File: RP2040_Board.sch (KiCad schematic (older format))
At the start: 1 part, among them U2 Pico

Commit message: Previous current input circuit was reaching op amp saturation. Possible solution may involve transistor, but for now, higher power supply is sufficient.
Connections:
- net labels added: +10V, 10V
- wire segments 12 -> 15
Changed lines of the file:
@@
 F3 "OUT" I R 7250 4050 50
 $EndSheet
+Text GLabel 2200 3550 1    50   Input ~ 0
+10V
+$Comp
+L power:PWR_FLAG #FLG?
+U 1 1 60AEFCD1
+P 2300 3600
+F 0 "#FLG?" H 2300 3675 50  0001 C CNN
+F 1 "PWR_FLAG" V 2300 3728 50  0000 L CNN
+F 2 "" H 2300 3600 50  0001 C CNN
+F 3 "~" H 2300 3600 50  0001 C CNN
+	1    2300 3600
+	0    1    1    0
+$EndComp
+$Comp
+L power:+10V #PWR?
+U 1 1 60AEFE56
+P 2200 3650
+F 0 "#PWR?" H 2200 3500 50  0001 C CNN
+F 1 "+10V" H 2215 3823 50  0000 C CNN
+F 2 "" H 2200 3650 50  0001 C CNN
+F 3 "" H 2200 3650 50  0001 C CNN
+	1    2200 3650
+	-1   0    0    1
+$EndComp
+Wire Wire Line
+	2200 3550 2200 3600
+Wire Wire Line
+	2300 3600 2200 3600
+Connection ~ 2200 3600
+Wire Wire Line
+	2200 3600 2200 3650
 $EndSCHEMATC

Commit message: Added Optically Isolated Digital Input
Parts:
- added J1: V_OUT, symbol Connector:Conn_01x02_Female
- added J2, J?: mA_OUT, symbol Connector:Conn_01x02_Female
- added J3: mA_IN, Connector_PinSocket_1.00mm:PinSocket_1x02_P1.00mm_Vertical, symbol Connector:Conn_01x02_Female
- added J4: V_IN, symbol Connector:Conn_01x02_Female
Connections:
- net labels added: +3.3V, 3.3V
- wire segments 15 -> 66
- no-connect marks 0 -> 36

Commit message: Comments and Notation for clarity
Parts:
- gave numbers to parts that had none: 1
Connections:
- net labels removed: +10V, 10V
- wire segments 66 -> 65
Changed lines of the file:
@@
 L power:+24V #PWR0102
 U 1 1 60A8325F
-P 1450 3000
-F 0 "#PWR0102" H 1450 2850 50  0001 C CNN
-F 1 "+24V" H 1465 3173 50  0000 C CNN
-F 2 "" H 1450 3000 50  0001 C CNN
-F 3 "" H 1450 3000 50  0001 C CNN
-	1    1450 3000
-	1    0    0    -1
-$EndComp
-Text GLabel 1450 3100 3    50   Input ~ 0
+P 1050 3250
+F 0 "#PWR0102" H 1050 3100 50  0001 C CNN
+F 1 "+24V" H 1065 3423 50  0000 C CNN
+F 2 "" H 1050 3250 50  0001 C CNN
+F 3 "" H 1050 3250 50  0001 C CNN
+	1    1050 3250
+	1    0    0    -1
+$EndComp
+Text GLabel 1050 3350 3    50   Input ~ 0
 24V
 Text GLabel 1050 3800 1    50   Input ~ 0
 GND
 Wire Wire Line
-	1450 3000 1450 3050
+	1050 3250 1050 3300
 Wire Wire Line
 	1050 3900 1050 3850
@@
 L power:PWR_FLAG #FLG0101
 U 1 1 60A8412B
-P 1550 3050
-F 0 "#FLG0101" H 1550 3125 50  0001 C CNN
-F 1 "PWR_FLAG" V 1550 3178 50  0000 L CNN
-F 2 "" H 1550 3050 50  0001 C CNN
-F 3 "~" H 1550 3050 50  0001 C CNN
-	1    1550 3050
+P 1150 3300
+F 0 "#FLG0101" H 1150 3375 50  0001 C CNN
+F 1 "PWR_FLAG" V 1150 3428 50  0000 L CNN
+F 2 "" H 1150 3300 50  0001 C CNN
+F 3 "~" H 1150 3300 50  0001 C CNN
+	1    1150 3300
 	0    1    1    0
 $EndComp
@@
 $EndComp
 Wire Wire Line
-	1550 3050 1450 3050
-Connection ~ 1450 3050
-Wire Wire Line
-	1450 3050 1450 3100
+	1150 3300 1050 3300
+Connection ~ 1050 3300
+Wire Wire Line
+	1050 3300 1050 3350
 Wire Wire Line
 	1150 3850 1050 3850
@@
 L power:+5V #PWR0103
 U 1 1 60A9FB68
-P 2150 3000
-F 0 "#PWR0103" H 2150 2850 50  0001 C CNN
-F 1 "+5V" H 2165 3173 50  0000 C CNN
-F 2 "" H 2150 3000 50  0001 C CNN
-F 3 "" H 2150 3000 50  0001 C CNN
-	1    2150 3000
-	1    0    0    -1
-$EndComp
-Text GLabel 2150 3100 3    50   Input ~ 0
+P 1800 3250
+F 0 "#PWR0103" H 1800 3100 50  0001 C CNN
+F 1 "+5V" H 1815 3423 50  0000 C CNN
+F 2 "" H 1800 3250 50  0001 C CNN
+F 3 "" H 1800 3250 50  0001 C CNN
+	1    1800 3250
+	1    0    0    -1
+$EndComp
+Text GLabel 1800 3350 3    50   Input ~ 0
 5V
 Wire Wire Line
-	2150 3000 2150 3050
+	1800 3250 1800 3300
 $Comp
 L power:PWR_FLAG #FLG0103
 U 1 1 60AA0BC3
-P 2250 3050
-F 0 "#FLG0103" H 2250 3125 50  0001 C CNN
-F 1 "PWR_FLAG" V 2250 3178 50  0000 L CNN
-F 2 "" H 2250 3050 50  0001 C CNN
-F 3 "~" H 2250 3050 50  0001 C CNN
-	1    2250 3050
+P 1900 3300
+F 0 "#FLG0103" H 1900 3375 50  0001 C CNN
+F 1 "PWR_FLAG" V 1900 3428 50  0000 L CNN
+F 2 "" H 1900 3300 50  0001 C CNN
+F 3 "~" H 1900 3300 50  0001 C CNN
+	1    1900 3300
 	0    1    1    0
 $EndComp
 Wire Wire Line
-	2250 3050 2150 3050
-Connection ~ 2150 3050
-Wire Wire Line
-	2150 3050 2150 3100
+	1900 3300 1800 3300
+Connection ~ 1800 3300
+Wire Wire Line
+	1800 3300 1800 3350
 Text GLabel 5750 4850 3    50   Input ~ 0
 GND
@@
 F3 "OUT" I L 4000 3000 50
 $EndSheet
-Text GLabel 750  3100 3    50   Input ~ 0
-10V
-$Comp
-L power:PWR_FLAG #FLG0104
-U 1 1 60AEFCD1
-P 850 3050
-F 0 "#FLG0104" H 850 3125 50  0001 C CNN
-F 1 "PWR_FLAG" V 850 3178 50  0000 L CNN
-F 2 "" H 850 3050 50  0001 C CNN
-F 3 "~" H 850 3050 50  0001 C CNN
-	1    850  3050
-	0    1    1    0
-$EndComp
-$Comp
-L power:+10V #PWR0104
-U 1 1 60AEFE56
-P 750 3000
-F 0 "#PWR0104" H 750 2850 50  0001 C CNN
-F 1 "+10V" H 765 3173 50  0000 C CNN
-F 2 "" H 750 3000 50  0001 C CNN
-F 3 "" H 750 3000 50  0001 C CNN
-	1    750  3000
-	1    0    0    -1
-$EndComp
 NoConn ~ 5050 2750
 NoConn ~ 5050 2950
@@
 F4 "OUT" I R 4600 3800 50
 $EndSheet
-Text GLabel 6550 2950 2    50   Input ~ 0
+Text GLabel 6550 2900 2    50   Input ~ 0
 3.3V
-Wire Wire Line
-	6450 2950 6550 2950
-Wire Wire Line
-	750  3000 750  3050
-Wire Wire Line
-	750  3050 850  3050
-Connection ~ 750  3050
-Wire Wire Line
-	750  3050 750  3100
 Text GLabel 1800 3800 1    50   Input ~ 0
 3.3V
@@
 	4950 2850 5050 2850
 $Comp
-L Connector:Conn_01x02_Female J?
+L Connector:Conn_01x02_Female J5
 U 1 1 60B47D03
 P 3550 3850
-F 0 "J?" H 3442 3525 50  0000 C CNN
+F 0 "J5" H 3442 3525 50  0000 C CNN
 F 1 "mA_OUT" H 3442 3616 50  0000 C CNN
 F 2 "" H 3550 3850 50  0001 C CNN
@@
 Wire Wire Line
 	3800 3750 3750 3750
+Wire Wire Line
+	6450 2950 6500 2950
+Wire Wire Line
+	6500 2950 6500 2900
+Wire Wire Line
+	6500 2900 6550 2900
 $EndSCHEMATC

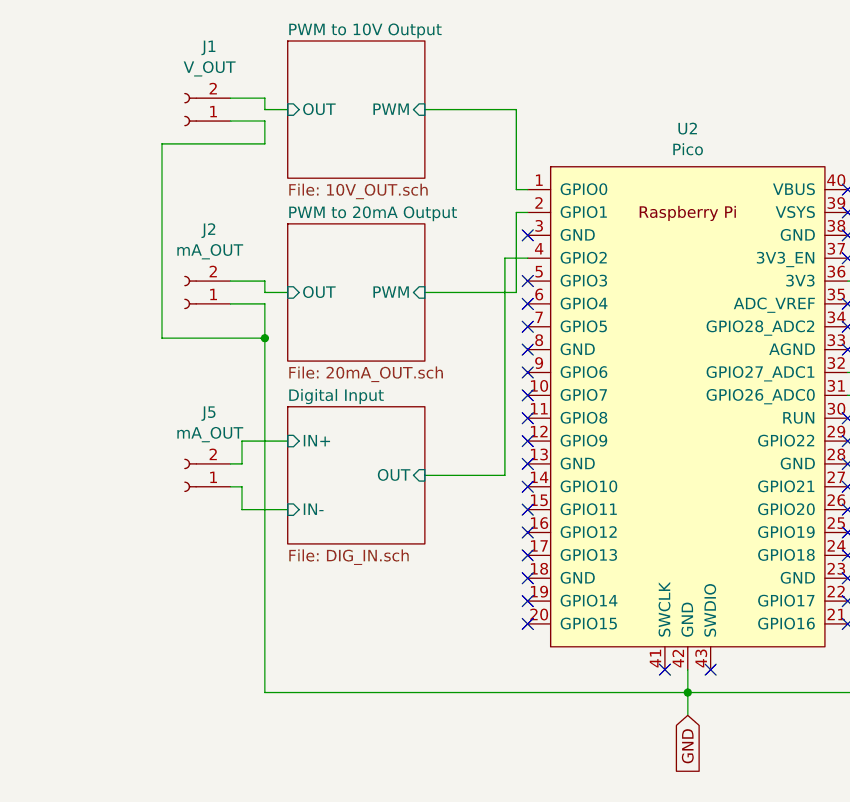
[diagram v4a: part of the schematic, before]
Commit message: Cleanup, added second digital input, and created sheet for digital output (currently empty)
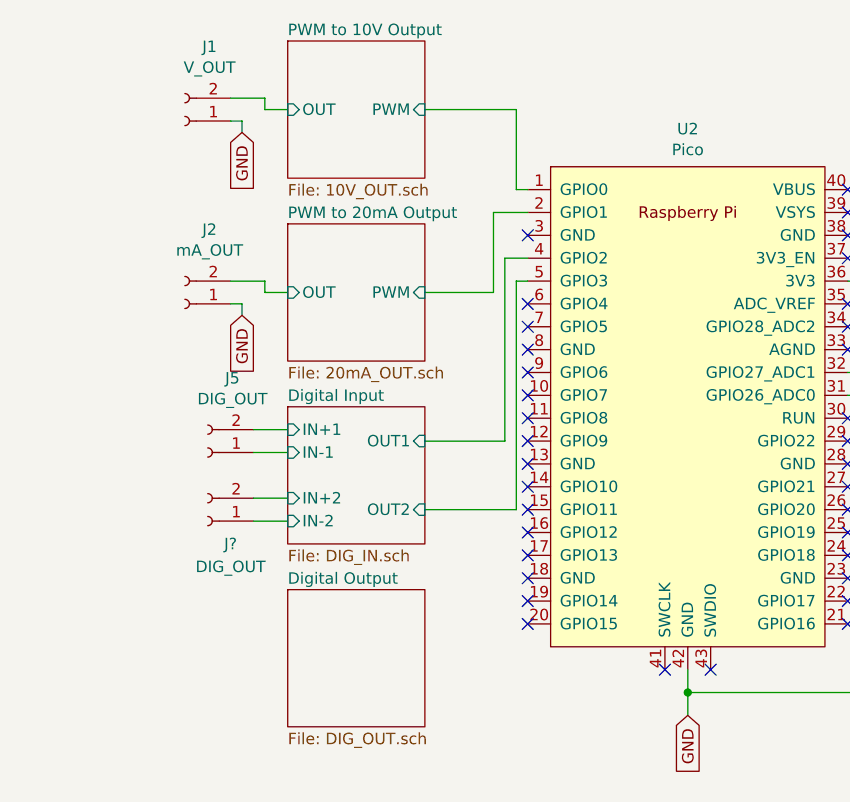
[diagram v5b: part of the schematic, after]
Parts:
- added J?: DIG_OUT, symbol Connector:Conn_01x02_Female
- J5: value mA_OUT -> DIG_OUT
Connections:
- net Digital Input/OUT2: now reaches U2.5 (GPIO3)
- net Digital Input/IN+ renamed Digital Input/IN+1
- net Digital Input/IN- renamed Digital Input/IN-1
- net Digital Input/OUT renamed Digital Input/OUT1
- new net Digital Input/IN+2: J?.2 (Pin_2)
- new net Digital Input/IN-2: J?.1 (Pin_1)
- no-connect marks 36 -> 35
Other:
- moved on the sheet: J5
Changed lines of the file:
@@
 $Descr A4 11693 8268
 encoding utf-8
-Sheet 1 6
+Sheet 1 7
 Title "Pi Pico Test Board"
 Date "2021-05-20"
@@
 $EndSheet
 NoConn ~ 5050 2750
-NoConn ~ 5050 2950
 NoConn ~ 5050 3050
 NoConn ~ 5050 3150
@@
 	5000 2200 4600 2200
 Wire Wire Line
-	5050 2650 5000 2650
-Wire Wire Line
-	5000 2650 5000 3000
-Wire Wire Line
-	5000 3000 4600 3000
-Wire Wire Line
 	6450 3350 6500 3350
 Wire Wire Line
@@
 $EndComp
 Wire Wire Line
-	5750 4750 3900 4750
-Wire Wire Line
-	3900 3050 3750 3050
-Wire Wire Line
 	4000 3000 3900 3000
 Wire Wire Line
@@
 Wire Wire Line
 	3900 2950 3750 2950
-Wire Wire Line
-	3900 4750 3900 3200
-Wire Wire Line
-	3900 3200 3450 3200
-Wire Wire Line
-	3450 3200 3450 2350
-Wire Wire Line
-	3450 2350 3900 2350
-Wire Wire Line
-	3900 2350 3900 2250
-Wire Wire Line
-	3900 2250 3750 2250
-Connection ~ 3900 3200
-Wire Wire Line
-	3900 3200 3900 3050
 $Sheet
 S 4000 3500 600  600
@@
 F0 "Digital Input" 50
 F1 "DIG_IN.sch" 50
-F2 "IN+" I L 4000 3650 50
-F3 "IN-" I L 4000 3950 50
-F4 "OUT" I R 4600 3800 50
+F2 "IN+1" I L 4000 3600 50
+F3 "IN-1" I L 4000 3700 50
+F4 "OUT1" I R 4600 3650 50
+F5 "IN+2" I L 4000 3900 50
+F6 "IN-2" I L 4000 4000 50
+F7 "OUT2" I R 4600 3950 50
 $EndSheet
 Text GLabel 6550 2900 2    50   Input ~ 0
@@
 	-1   0    0    1
 $EndComp
-Wire Wire Line
-	4600 3800 4950 3800
-Wire Wire Line
-	4950 3800 4950 2850
-Wire Wire Line
-	4950 2850 5050 2850
 $Comp
 L Connector:Conn_01x02_Female J5
 U 1 1 60B47D03
-P 3550 3850
-F 0 "J5" H 3442 3525 50  0000 C CNN
-F 1 "mA_OUT" H 3442 3616 50  0000 C CNN
-F 2 "" H 3550 3850 50  0001 C CNN
-F 3 "~" H 3550 3850 50  0001 C CNN
-	1    3550 3850
+P 3650 3700
+F 0 "J5" H 3542 3375 50  0000 C CNN
+F 1 "DIG_OUT" H 3542 3466 50  0000 C CNN
+F 2 "" H 3650 3700 50  0001 C CNN
+F 3 "~" H 3650 3700 50  0001 C CNN
+	1    3650 3700
 	-1   0    0    1
 $EndComp
 Wire Wire Line
-	4000 3950 3800 3950
-Wire Wire Line
-	3800 3950 3800 3850
-Wire Wire Line
-	3800 3850 3750 3850
-Wire Wire Line
-	4000 3650 3800 3650
-Wire Wire Line
-	3800 3650 3800 3750
-Wire Wire Line
-	3800 3750 3750 3750
-Wire Wire Line
 	6450 2950 6500 2950
 Wire Wire Line
@@
 Wire Wire Line
 	6500 2900 6550 2900
+Wire Wire Line
+	5050 2950 5000 2950
+Wire Wire Line
+	5000 2950 5000 3950
+Wire Wire Line
+	5000 3950 4600 3950
+Wire Wire Line
+	5050 2850 4950 2850
+Wire Wire Line
+	4950 2850 4950 3650
+Wire Wire Line
+	4950 3650 4600 3650
+Wire Wire Line
+	5050 2650 4900 2650
+Wire Wire Line
+	4900 2650 4900 3000
+Wire Wire Line
+	4900 3000 4600 3000
+$Comp
+L Connector:Conn_01x02_Female J?
+U 1 1 60BADF7F
+P 3650 4000
+F 0 "J?" H 3550 4100 50  0000 C CNN
+F 1 "DIG_OUT" H 3550 4200 50  0000 C CNN
+F 2 "" H 3650 4000 50  0001 C CNN
+F 3 "~" H 3650 4000 50  0001 C CNN
+	1    3650 4000
+	-1   0    0    1
+$EndComp
+Wire Wire Line
+	4000 3600 3850 3600
+Wire Wire Line
+	4000 3700 3850 3700
+Wire Wire Line
+	4000 3900 3850 3900
+Wire Wire Line
+	4000 4000 3850 4000
+Text GLabel 3800 3100 3    50   Input ~ 0
+GND
+Text GLabel 3800 2300 3    50   Input ~ 0
+GND
+Wire Wire Line
+	3800 2300 3800 2250
+Wire Wire Line
+	3800 2250 3750 2250
+Wire Wire Line
+	3800 3100 3800 3050
+Wire Wire Line
+	3800 3050 3750 3050
+$Sheet
+S 4000 4300 600  600
+U 60BBF151
+F0 "Digital Output" 50
+F1 "DIG_OUT.sch" 50
+$EndSheet
 $EndSCHEMATC

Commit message: Testing and adjustments
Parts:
- gave numbers to parts that had none: 1
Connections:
- net +3V3 renamed 3.3V
- net GNDREF renamed GND
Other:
- moved on the sheet: J1, J2, J3, J4, J5, J6, U2

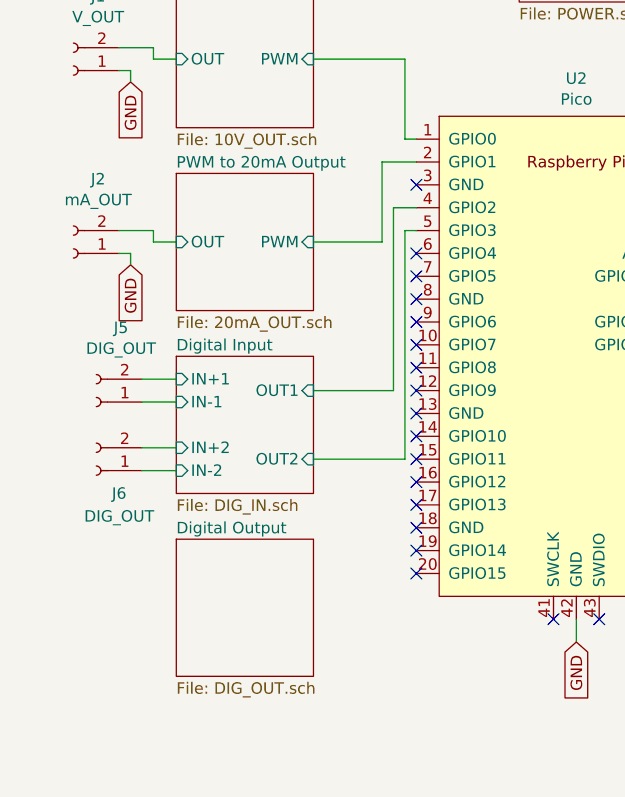
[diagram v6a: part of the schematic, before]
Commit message: Basic Digital Output Circuit (First Revision, UNTESTED)
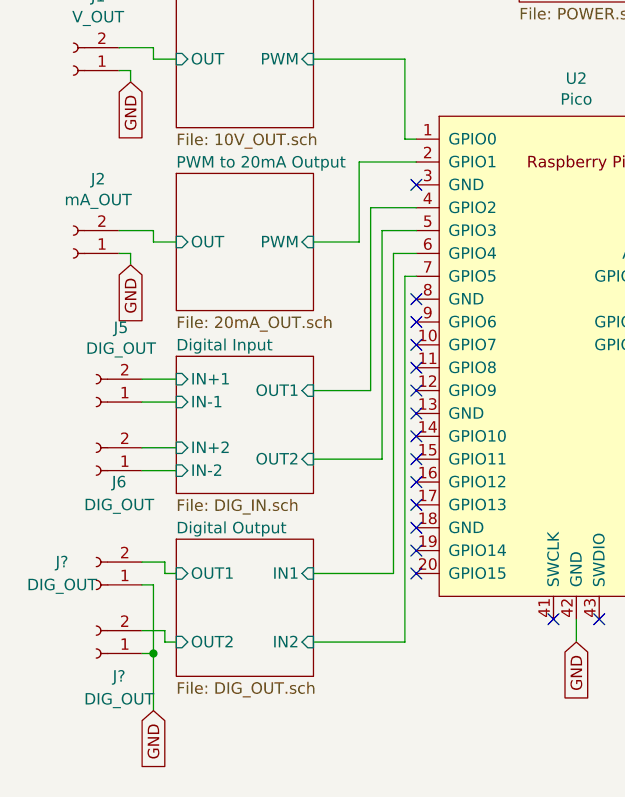
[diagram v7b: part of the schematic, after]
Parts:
- added J? (x2): DIG_OUT, symbol Connector:Conn_01x02_Female
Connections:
- net GND: now also J?.1 (Pin_1), J?.1 (Pin_1)
- net Digital Output/IN1: now reaches U2.6 (GPIO4)
- net Digital Output/IN2: now reaches U2.7 (GPIO5)
- new net Digital Output/OUT1: J?.2 (Pin_2)
- new net Digital Output/OUT2: J?.2 (Pin_2)
- no-connect marks 35 -> 33
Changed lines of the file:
@@
 $EndSheet
 NoConn ~ 5200 3350
-NoConn ~ 5200 3650
-NoConn ~ 5200 3750
 NoConn ~ 5200 3850
 NoConn ~ 6600 3150
@@
 Wire Wire Line
 	6650 3500 6700 3500
-Wire Wire Line
-	5200 3550 5150 3550
-Wire Wire Line
-	5150 3550 5150 4550
-Wire Wire Line
-	5150 4550 4750 4550
-Wire Wire Line
-	5200 3450 5100 3450
-Wire Wire Line
-	5100 3450 5100 4250
-Wire Wire Line
-	5100 4250 4750 4250
-Wire Wire Line
-	5200 3250 5050 3250
-Wire Wire Line
-	5050 3250 5050 3600
-Wire Wire Line
-	5050 3600 4750 3600
 $Comp
 L Connector:Conn_01x02_Female J6
 U 1 1 60BADF7F
 P 3800 4600
-F 0 "J6" H 3700 4700 50  0000 C CNN
-F 1 "DIG_OUT" H 3700 4800 50  0000 C CNN
+F 0 "J6" H 3700 4650 50  0000 C CNN
+F 1 "DIG_OUT" H 3700 4750 50  0000 C CNN
 F 2 "" H 3800 4600 50  0001 C CNN
 F 3 "~" H 3800 4600 50  0001 C CNN
@@
 Wire Wire Line
 	3950 3650 3900 3650
+Wire Wire Line
+	5900 5350 5900 5250
+Text GLabel 7850 4500 3    50   Input ~ 0
+GND
+Wire Wire Line
+	7900 4450 7850 4450
+Wire Wire Line
+	7850 4450 7850 4500
+$Sheet
+S 5650 1950 600  600
+U 60BF1335
+F0 "Power Supply" 50
+F1 "POWER.sch" 50
+$EndSheet
 $Sheet
 S 4150 4900 600  600
@@
 F0 "Digital Output" 50
 F1 "DIG_OUT.sch" 50
-$EndSheet
-Wire Wire Line
-	5900 5350 5900 5250
-Text GLabel 7850 4500 3    50   Input ~ 0
+F2 "OUT1" I L 4150 5050 50
+F3 "IN1" I R 4750 5050 50
+F4 "IN2" I R 4750 5350 50
+F5 "OUT2" I L 4150 5350 50
+$EndSheet
+Wire Wire Line
+	5200 3750 5150 3750
+Wire Wire Line
+	5150 3750 5150 5350
+Wire Wire Line
+	5150 5350 4750 5350
+Wire Wire Line
+	5200 3650 5100 3650
+Wire Wire Line
+	5100 3650 5100 5050
+Wire Wire Line
+	5100 5050 4750 5050
+Wire Wire Line
+	5200 3550 5050 3550
+Wire Wire Line
+	5050 3550 5050 4550
+Wire Wire Line
+	5050 4550 4750 4550
+Wire Wire Line
+	5200 3450 5000 3450
+Wire Wire Line
+	5000 3450 5000 4250
+Wire Wire Line
+	5000 4250 4750 4250
+Wire Wire Line
+	5200 3250 4950 3250
+Wire Wire Line
+	4950 3250 4950 3600
+Wire Wire Line
+	4950 3600 4750 3600
+$Comp
+L Connector:Conn_01x02_Female J?
+U 1 1 60C380A7
+P 3800 5100
+F 0 "J?" H 3950 5000 50  0000 C CNN
+F 1 "DIG_OUT" H 3950 5100 50  0000 C CNN
+F 2 "" H 3800 5100 50  0001 C CNN
+F 3 "~" H 3800 5100 50  0001 C CNN
+	1    3800 5100
+	-1   0    0    1
+$EndComp
+$Comp
+L Connector:Conn_01x02_Female J?
+U 1 1 60C39103
+P 3800 5400
+F 0 "J?" H 3700 5500 50  0000 C CNN
+F 1 "DIG_OUT" H 3700 5600 50  0000 C CNN
+F 2 "" H 3800 5400 50  0001 C CNN
+F 3 "~" H 3800 5400 50  0001 C CNN
+	1    3800 5400
+	-1   0    0    1
+$EndComp
+Text GLabel 4050 5650 3    50   Input ~ 0
 GND
 Wire Wire Line
-	7900 4450 7850 4450
-Wire Wire Line
-	7850 4450 7850 4500
-$Sheet
-S 5650 1950 600  600
-U 60BF1335
-F0 "Power Supply" 50
-F1 "POWER.sch" 50
-$EndSheet
+	4150 5350 4100 5350
+Wire Wire Line
+	4100 5350 4100 5300
+Wire Wire Line
+	4100 5300 4000 5300
+Wire Wire Line
+	4150 5050 4100 5050
+Wire Wire Line
+	4100 5050 4100 5000
+Wire Wire Line
+	4100 5000 4000 5000
+Wire Wire Line
+	4050 5650 4050 5400
+Wire Wire Line
+	4050 5100 4000 5100
+Wire Wire Line
+	4050 5400 4000 5400
+Connection ~ 4050 5400
+Wire Wire Line
+	4050 5400 4050 5100
 $EndSCHEMATC
